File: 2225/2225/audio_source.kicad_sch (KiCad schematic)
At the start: 2 parts

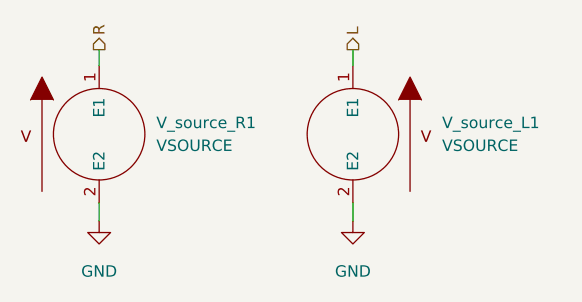
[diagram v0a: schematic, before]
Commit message: Initial system block diagram of 2225
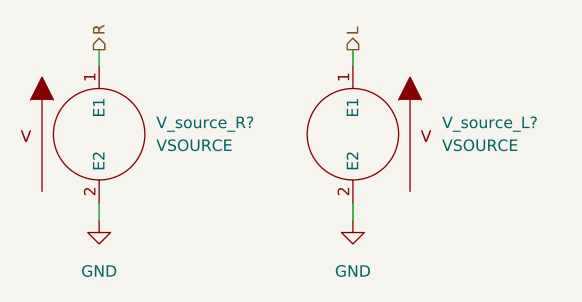
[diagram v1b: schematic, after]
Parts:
- renumbered V_source_L1 to V_source_L?, V_source_R1 to V_source_R?
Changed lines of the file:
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@@
   (symbol (lib_id "power:GND") (at 152.654 106.426 0) (unit 1)
     (in_bom yes) (on_board yes) (fields_autoplaced)
-    (property "Reference" "#PWR0114" (id 0) (at 152.654 112.776 0)
+    (property "Reference" "#PWR?" (id 0) (at 152.654 112.776 0)
       (effects (font (size 1.27 1.27)) hide)
     )
@@
   (symbol (lib_id "pspice:VSOURCE") (at 152.654 96.774 0) (mirror y) (unit 1)
     (in_bom yes) (on_board yes) (fields_autoplaced)
-    (property "Reference" "V_source_L1" (id 0) (at 162.56 95.5039 0)
+    (property "Reference" "V_source_L?" (id 0) (at 162.56 95.5039 0)
       (effects (font (size 1.27 1.27)) (justify right))
     )
@@
   (symbol (lib_id "pspice:VSOURCE") (at 124.46 96.774 0) (unit 1)
     (in_bom yes) (on_board yes) (fields_autoplaced)
-    (property "Reference" "V_source_R1" (id 0) (at 130.81 95.5039 0)
+    (property "Reference" "V_source_R?" (id 0) (at 130.81 95.5039 0)
       (effects (font (size 1.27 1.27)) (justify left))
     )
@@
   (symbol (lib_id "power:GND") (at 124.46 106.426 0) (unit 1)
     (in_bom yes) (on_board yes) (fields_autoplaced)
-    (property "Reference" "#PWR0115" (id 0) (at 124.46 112.776 0)
+    (property "Reference" "#PWR?" (id 0) (at 124.46 112.776 0)
       (effects (font (size 1.27 1.27)) hide)
     )
